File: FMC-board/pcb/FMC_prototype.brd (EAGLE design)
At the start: 76.5 x 69 mm, 90 parts, among them U1 4901, U2 TPS79333, U3 ADN4663, U4 ADN4663, U5 ADN4664, U6 PDS1-S12-S5-S, U8 4901

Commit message: More silkscreen fixes and test points
- Added test pads for digital lines on paths through isolation
  circuitry. Used small inline padsto prevent stubs.
- Silkscreen looks pretty good now.
- Boards needs a fresh look over then fab, I think.
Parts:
- removed C33: 1nF, jonnew:0603
- removed C34: 10uF, jonnew:1206-POL
- removed C40: 10uF, puggleboard:1206
- removed R17: 10k, jonnew:0603
- removed U$1: OPEN_EPHYS_LOGO, open-ephys:OPEN_EPHYS_LOGO
- removed U$2: FMC_SINGLE_WIDTH_MODULE, jonnew:FMC_SINGLE_WIDTH_MODULE
- added C19: 2.2uF, jonnew:1206
- added C25: 100nF, RHD2000_eval_board:0603
- added C26: 22uF, jonnew:1210-POL
- added PWR_ISO: 569-011x, jonnew:569-011X-X00_LED_ARRAY
- added R15: 100, jonnew:0603
- added TP1: GND-ISO, jonnew:TP06R
- added TP10: SCLK-, jonnew:TP06R
- added TP11: CS+, jonnew:TP06R
- added TP12: CS-, jonnew:TP06R
- added TP3: MISO2+, jonnew:TP06R
- added TP4: MISO2-, jonnew:TP06R
- added TP5: MISO1+, jonnew:TP06R
- added TP6: MISO1-, jonnew:TP06R
- added TP7: MOSI+, jonnew:TP06R
- added TP8: MOSI-, jonnew:TP06R
- added TP9: SCLK+, jonnew:TP06R
- added TP_CS: CS, jonnew:TP06R
- added TP_H13: H13, jonnew:TP06R
- added TP_H14: H14, jonnew:TP06R
- added TP_H23: H23, jonnew:TP06R
- added TP_MISO1: MISO1, jonnew:TP06R
- added TP_MISO2: MISO2, jonnew:TP06R
- added TP_MOSI: MOSI, jonnew:TP06R
- added TP_SCLK: SCLK, jonnew:TP06R
- added U7: 4901, puggleboard:SOP65P490X110-9N
- C10: value 1.0u -> 100nF; device RHD2000_eval_board:0805 -> RHD2000_eval_board:0603
- C11: value 10uF -> 1nF; device jonnew:1206 -> jonnew:0603
- C12: value 100n -> 10uF; device RHD2000_eval_board:0603 -> puggleboard:1206
- C13: value 100n -> 1.0uF; device RHD2000_eval_board:0603 -> RHD2000_eval_board:0805
- C14: value 100n -> 10uF; device RHD2000_eval_board:0603 -> jonnew:1206
- C15, C8: value 100n -> 100nF
- C16: value 1nF -> 100nF; device jonnew:0603 -> RHD2000_eval_board:0603
- C18: value 2.2uF -> 100nF; device jonnew:1206 -> RHD2000_eval_board:0603
- C2: value 10uF -> 10nF; device puggleboard:1206 -> jonnew:0603
- C20, C24: value 100nF -> 10uF; device RHD2000_eval_board:0603 -> puggleboard:1206
- C21: value 10uF -> 1nF; device puggleboard:1206 -> jonnew:0603
- C28: value 100n -> 22uF; device RHD2000_eval_board:0603 -> jonnew:1210-POL
- C3: value 22u -> 22uF
- C30, C31: value 22uF -> 100nF; device jonnew:1210-POL -> RHD2000_eval_board:0603
- C32: value 10uF -> 100nF; device jonnew:1206-POL -> RHD2000_eval_board:0603
- C4: value 10nF -> 10uF; device jonnew:0603 -> jonnew:1206-POL
- C5: value 10n -> 10uF; device RHD2000_eval_board:0603 -> jonnew:1206-POL
- C6: value 100n -> 10nF
- C7: value 100n -> 10nF; device RHD2000_eval_board:0603 -> jonnew:0603
- C9: value 10nF -> 100nF; device jonnew:0603 -> RHD2000_eval_board:0603
- D4: value 8V -> STPS0560Z; device jonnew:SOD-323 -> jonnew:SOD123
- D7: value STPS0560Z -> BZT52C7V5
- DO_ISO: value IS07640 -> ISO7640
- H13, H14, H23: value 142-0701 -> SMA002
- R1, R16: value 20k -> 100
- R10, R11: value 100 -> 10k
- R12: value 100 -> 20k
- R13, R3: device RHD2000_eval_board:0603 -> jonnew:0603
- R2: value 820 -> 100; device RHD2000_eval_board:0603 -> jonnew:0603
- R4: value 100 -> 820
- R5: value 10k -> 20k
- R6: value 820 -> 10k; device RHD2000_eval_board:0603 -> jonnew:0603
- R7: value 10k -> 820
- R8, R9: device jonnew:0603 -> RHD2000_eval_board:0603
- U$3: value (none) -> OPEN_EPHYS_LOGO; device jonnew:569-011X-X00_LED_ARRAY -> open-ephys:OPEN_EPHYS_LOGO
- U2: value TPS79333 -> 7933
- U6: value PDS1-S12-S5-S -> PDS1
- U8: value 4901 -> FMC_SINGLE_WIDTH_MODULE; device puggleboard:SOP65P490X110-9N -> jonnew:FMC_SINGLE_WIDTH_MODULE
- moved U$16 69.3 mm to (95.4, 39.9)
- moved C24 58.0 mm to (-29.5, 7.87), flipped to the top, turned to 270 degrees
- moved C32 53.1 mm to (6.35, 50.3), flipped to the bottom, turned to 270 degrees
- moved R14 50.9 mm to (-17.5, 54.9), flipped to the top, turned to 90 degrees
- moved D13 50.8 mm to (-9.91, 48.8), flipped to the top
- moved D5 50.8 mm to (-51.3, 19.3), flipped to the bottom
- moved D11 49.5 mm to (-9.91, 43.4), flipped to the top, turned to 270 degrees
- moved C20 48.0 mm to (-20.6, 7.87), flipped to the top, turned to 270 degrees
- moved D7 47.7 mm to (-37.3, 7.87), turned to 0 degrees
- moved D6 47.0 mm to (-53.1, 19.3), flipped to the bottom, turned to 90 degrees
- moved R16 44.9 mm to (-28.2, 53.3), turned to 90 degrees
- moved D3 44.4 mm to (-51.3, 27.4), flipped to the bottom
- moved R9 44.3 mm to (-42.2, 18.0), turned to 270 degrees
- moved D12 44.1 mm to (-12.7, 48.8), flipped to the top
- moved D10 43.4 mm to (-12.7, 43.4), flipped to the top, turned to 270 degrees
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- renumbered C35 to C22, C37 to C23, C_ISOLATED to C_ISO, G1 to G21, G2 to G22, G3 to G24, U$4 to Q1
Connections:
- removed net C10: FMC.P$130
- removed net C11: FMC.P$131
- removed net C14: FMC.P$134
- removed net C18: FMC.P$138
- removed net N$9: FMC.P$76
- removed net TP7: FMC.P$135
- net +3V3: now also C18.2, C25.2, C29.2, C31.2, D10.C, D12.C, D8.C; no longer C14.2, C15.2, C20.2, C24.2, D2.C, D6.C, D7.C
- net +3V3_ISO: now also C10.1, C15.2, C16.2, C4.+, C5.+, C9.1, D1.C, D3.C, D5.C, R7.1; no longer C12.2, C13.2, C32.+, C34.+, C6.1, C7.1, D12.C, D13.C, D8.C, R2.1
- net +3V6: now also C24.1, R12.1, U7.1; no longer C40.1, R16.1, U8.1
- net +3V6_ISO: now also C1.1, R4.1, R5.1; no longer C4.1, R1.1, R6.1
- net +5V0_ISO: now also C11.1, C12.1, C13.1; no longer C1.1, C10.1, C16.1
- net +5V0_ISO-PRE: now also C14.1; no longer C11.1
- net 12V_FPGA: now also C19.1, C26.+, C28.+, C30.2, C32.2; no longer C18.1, C28.2, C29.2, C30.+, C31.+
- net AGND1: now also R12.2, R13.1, U7.2; no longer R16.2, R17.1, U8.2
- net AGND2: now also C2.2, R5.2, R6.1; no longer C4.2, R1.2, R5.1
- net CS: now also TP_CS.TP
- net CS+_ISOLATED: now also TP11.TP
- net CS-_ISOLATED: now also TP12.TP
- net G21: now also D8.A, D9.C, R16.1; no longer D1.C, D2.A, R8.1
- net G22: now also D10.A, D11.C, R14.1; no longer D3.C, D6.A, R9.1
- net G24: now also D12.A, D13.C, R15.1; no longer D5.C, D7.A, R10.1
- net GND: now also C18.1, C19.2, C20.2, C24.2, C25.1, C26.-, C28.-, C30.1, C31.1, C32.1, D11.A, D13.A, D9.A, R11.1, R13.2, U7.4, U7.9; no longer C14.1, C15.1, C18.2, C20.1, C24.1, C28.1, C30.-, C31.-, C33.2, C40.2, D1.A, D3.A, D5.A, R13.1, R17.2, U8.4, U8.9
- net GND_ISO: now also C12.2, C13.2, C14.2, C15.1, C16.1, C4.-, C5.-, D2.A, D4.A, D6.A, PWR_ISO.C1, PWR_ISO.C2, R10.1, R6.2, TP1.TP; no longer C12.1, C13.1, C16.2, C2.2, C32.-, C34.-, C5.2, D10.A, D11.A, D9.A, R5.2, R7.1, U$3.C1, U$3.C2
- net H13: now also TP_H13.TP
- net H13_ISO: now also D5.A, D6.C, R3.1; no longer D11.C, D13.A, R14.1
- net H14: now also TP_H14.TP
- net H14_ISO: now also D3.A, D4.C, R2.1; no longer D10.C, D12.A, R12.1
- net H23: now also TP_H23.TP
- net H23_ISO: now also D1.A, D2.C, R1.1; no longer D8.A, D9.C, R11.1
- net MISO1: now also TP_MISO1.TP
- net MISO1+_ISOLATED: now also R9.1, TP5.TP; no longer R4.1
- net MISO1-_ISOLATED: now also R9.2, TP6.TP; no longer R4.2
- net MISO2: now also TP_MISO2.TP
- net MISO2+_ISOLATED: now also R8.1, TP3.TP; no longer R3.1
- net MISO2-_ISOLATED: now also R8.2, TP4.TP; no longer R3.2
- net MOSI: now also TP_MOSI.TP
- net N$1: now also U7.6; no longer U8.6
- net N$10: now also PWR_ISO.A1, R7.2; no longer R2.2, U$3.A1
- net N$11: now also R1.2; no longer R11.2
- net N$12: now also TP7.TP
- net N$13: now also TP8.TP
- net N$14: now also R2.2; no longer R12.2
- net N$15: now also TP9.TP
- net N$16: now also TP10.TP
- net N$17: now also R3.2; no longer R14.2
- net N$18: now also R14.2; no longer R9.2
- net N$19: now also R15.2; no longer R10.2
- net N$2: now also R16.2; no longer R8.2
- net N$3: now also D7.C; no longer D4.C
- net N$4: now also C7.1; no longer C9.1
- net N$5: now also R10.2; no longer R7.2
- net N$6: now also D7.A, R11.2; no longer D4.A, R13.2
- net N$8: now also PWR_ISO.A2, R4.2; no longer R6.2, U$3.A2
- net N$97: now also C6.1; no longer C5.1
- net SCLK: now also TP_SCLK.TP
- net VDD_POST_LC: now also C20.1, U7.5, U7.8; no longer C33.1, U8.5, U8.8
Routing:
- net GND_ISO: track 39.3 -> 43.4 mm, vias 33 -> 34
- net N$7: track 4.69 -> 7.02 mm
- net N$6: track 3.36 -> 5.34 mm
- net H13_ISO: track 28.0 -> 29.6 mm
- net +3V6: track 251.6 -> 250.6 mm
- net N$3: track 25.8 -> 26.4 mm
- net +3V3_ISO: track 32.3 -> 32.9 mm
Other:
- board text added: "+"
- board text added: "-"
- board text added: "COMMON"
- board text added: "FMC IO Module Rev. 0.1 2016.03"
- board text added: "FPGA_12v"
- board text added: "GND"
- board text added: "VDD_AUX"
- board text removed: "1_to_fpga"
- board text removed: "2_to_fpga"
- board text removed: "3.6v_hs"
- board text removed: "3_from_fpga"
- board text removed: "3v_fpga"
- board text removed: "5V isolated"
- board text removed: "FMC prototype board for"
- board text removed: "RHD headstages rev. 0.1"
- board text removed: "b_cs+"
- board text removed: "b_miso1+"
- board text removed: "b_miso2+"
- board text removed: "b_mosi+"
- board text removed: "b_sclk+"
- board text removed: "gnd"
- board text removed: "miso1+"
- board text removed: "miso1_se"
- board text removed: "mosi+"
- board text removed: "mosi_se"
- board text removed: "non-isolated"
- board text removed: "vdd33"
- board text removed: "vdd_in"
- board text removed: "vdd_is"

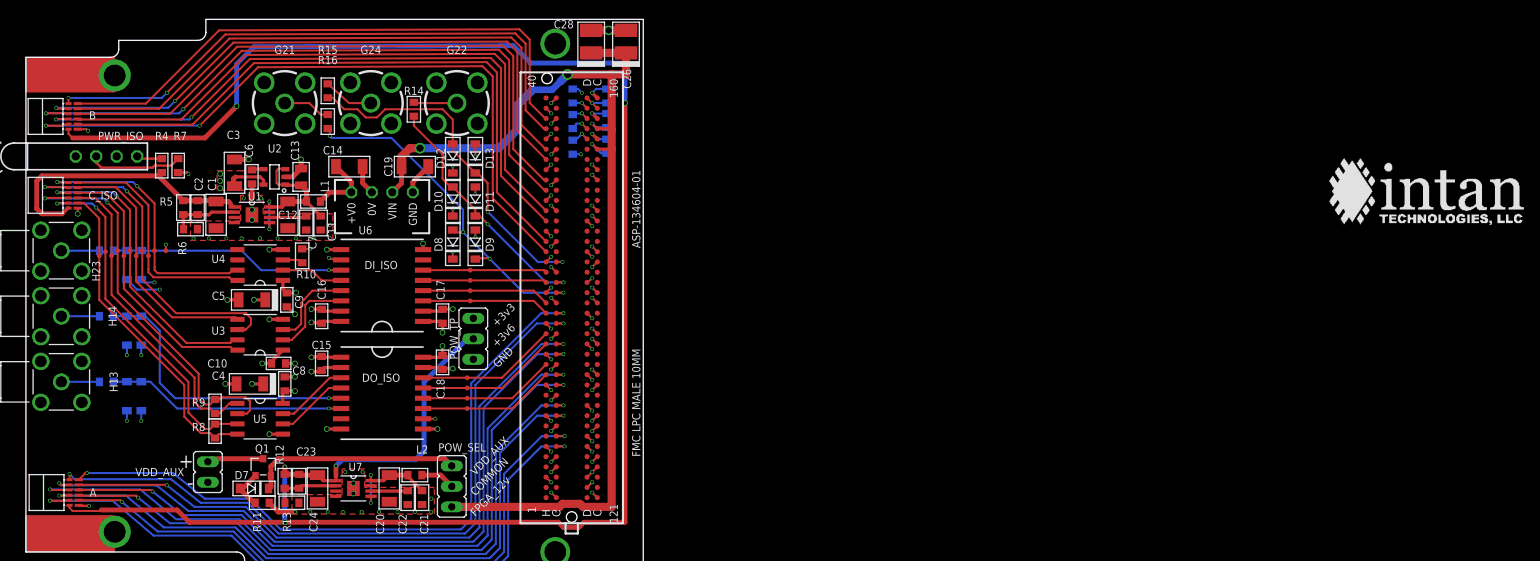
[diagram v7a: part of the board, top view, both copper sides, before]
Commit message: some small cleanups and added some silkscreen labels
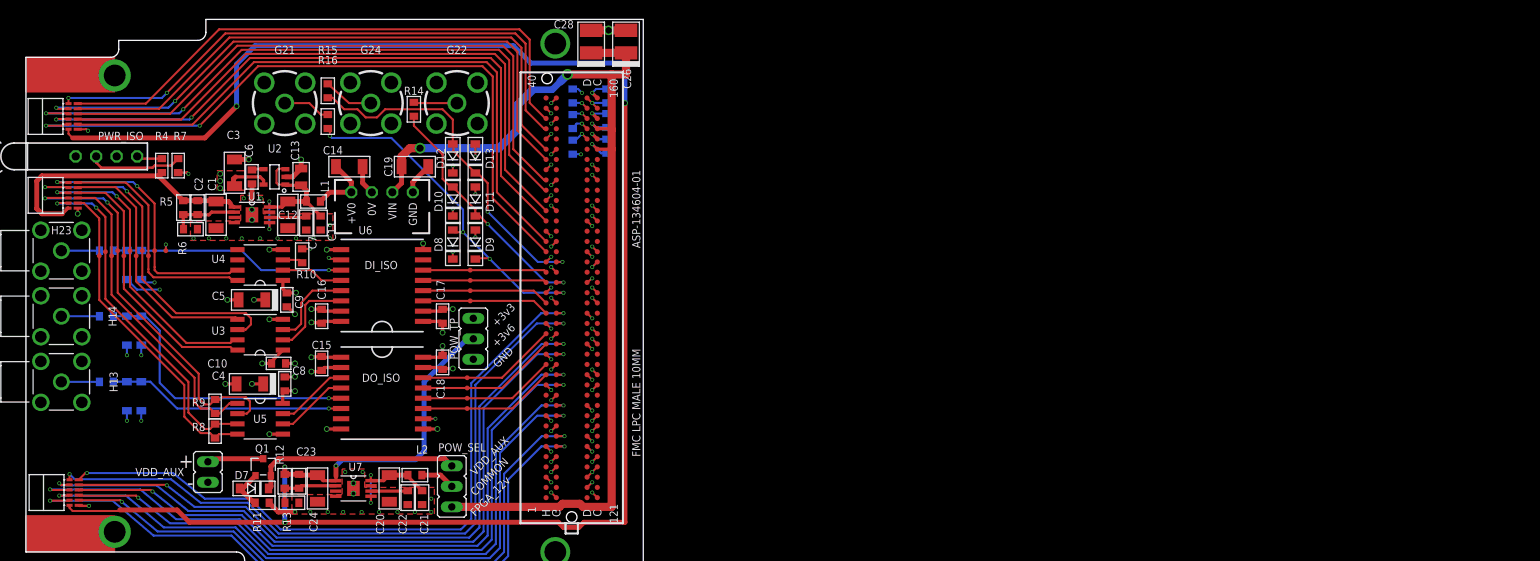
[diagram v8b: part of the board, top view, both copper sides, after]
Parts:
- removed U$16: (no value), RHD2000_eval_board:INTAN_LOGO
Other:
- board text added: "direct_fpga 3.3V ONLY"
- board text added: "direct_fpga_G21"
- board text added: "direct_fpga_G22"
- board text added: "direct_fpga_H1G24 3.3V ONLY"
- board text added: "from_fpga_H23"
- board text added: "to_fpga_H13"
- board text added: "to_fpga_H14"
